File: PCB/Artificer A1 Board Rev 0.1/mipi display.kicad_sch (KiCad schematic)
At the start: 0 parts

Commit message: added a few accessories
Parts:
- added FPC1, FPC2: 0.5K-A-22PB, easyeda:FPC-SMD_22P-P1.00_0.5K-A-22PB, symbol easyeda:0.5K-A-22PB
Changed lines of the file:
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@@
 		(company "Matthew Spotten")
 	)
+	(symbol
+		(lib_id "easyeda:0.5K-A-22PB")
+		(at 158.75 151.13 0)
+		(unit 1)
+		(exclude_from_sim no)
+		(in_bom yes)
+		(on_board yes)
+		(dnp no)
+		(fields_autoplaced yes)
+		(property "Reference" "FPC2"
+			(at 162.56 147.3199 0)
+			(effects
+				(font
+					(size 1.27 1.27)
+				)
+				(justify left)
+			)
+		)
+		(property "Value" "0.5K-A-22PB"
+			(at 162.56 149.8599 0)
+			(effects
+				(font
+					(size 1.27 1.27)
+				)
+				(justify left)
+			)
+		)
+		(property "Footprint" "easyeda:FPC-SMD_22P-P1.00_0.5K-A-22PB"
+			(at 158.75 190.5 0)
+			(effects
+				(font
+					(size 1.27 1.27)
+				)
+				(hide yes)
+			)
+		)
+		(property "Datasheet" ""
+			(at 158.75 151.13 0)
+			(effects
+				(font
+					(size 1.27 1.27)
+				)
+				(hide yes)
+			)
+		)
+		(property "Description" ""
+			(at 158.75 151.13 0)
+			(effects
+				(font
+					(size 1.27 1.27)
+				)
+				(hide yes)
+			)
+		)
+		(property "LCSC Part" "C2914146"
+			(at 158.75 193.04 0)
+			(effects
+				(font
+					(size 1.27 1.27)
+				)
+				(hide yes)
+			)
+		)
+		(pin "14"
+		)
+		(pin "17"
+		)
+		(pin "19"
+		)
+		(pin "3"
+		)
+		(pin "5"
+		)
+		(pin "10"
+		)
+		(pin "1"
+		)
+		(pin "16"
+		)
+		(pin "8"
+		)
+		(pin "6"
+		)
+		(pin "9"
+		)
+		(pin "22"
+		)
+		(pin "12"
+		)
+		(pin "2"
+		)
+		(pin "4"
+		)
+		(pin "7"
+		)
+		(pin "13"
+		)
+		(pin "11"
+		)
+		(pin "15"
+		)
+		(pin "18"
+		)
+		(pin "20"
+		)
+		(pin "21"
+		)
+		(pin "24"
+		)
+		(pin "23"
+		)
+		(instances
+			(project ""
+				(path "/7c37bdb5-94b0-4567-b5ec-a879db855389/f6f33ebb-5c0b-4a90-8c47-ad37181a309f"
+					(reference "FPC2")
+					(unit 1)
+				)
+			)
+		)
+	)
+	(symbol
+		(lib_id "easyeda:0.5K-A-22PB")
+		(at 232.41 60.96 0)
+		(unit 1)
+		(exclude_from_sim no)
+		(in_bom yes)
+		(on_board yes)
+		(dnp no)
+		(fields_autoplaced yes)
+		(property "Reference" "FPC1"
+			(at 236.22 57.1499 0)
+			(effects
+				(font
+					(size 1.27 1.27)
+				)
+				(justify left)
+			)
+		)
+		(property "Value" "0.5K-A-22PB"
+			(at 236.22 59.6899 0)
+			(effects
+				(font
+					(size 1.27 1.27)
+				)
+				(justify left)
+			)
+		)
+		(property "Footprint" "easyeda:FPC-SMD_22P-P1.00_0.5K-A-22PB"
+			(at 232.41 100.33 0)
+			(effects
+				(font
+					(size 1.27 1.27)
+				)
+				(hide yes)
+			)
+		)
+		(property "Datasheet" ""
+			(at 232.41 60.96 0)
+			(effects
+				(font
+					(size 1.27 1.27)
+				)
+				(hide yes)
+			)
+		)
+		(property "Description" ""
+			(at 232.41 60.96 0)
+			(effects
+				(font
+					(size 1.27 1.27)
+				)
+				(hide yes)
+			)
+		)
+		(property "LCSC Part" "C2914146"
+			(at 232.41 102.87 0)
+			(effects
+				(font
+					(size 1.27 1.27)
+				)
+				(hide yes)
+			)
+		)
+		(pin "2"
+		)
+		(pin "6"
+		)
+		(pin "1"
+		)
+		(pin "5"
+		)
+		(pin "12"
+		)
+		(pin "8"
+		)
+		(pin "4"
+		)
+		(pin "3"
+		)
+		(pin "7"
+		)
+		(pin "9"
+		)
+		(pin "10"
+		)
+		(pin "11"
+		)
+		(pin "22"
+		)
+		(pin "24"
+		)
+		(pin "19"
+		)
+		(pin "14"
+		)
+		(pin "15"
+		)
+		(pin "16"
+		)
+		(pin "23"
+		)
+		(pin "17"
+		)
+		(pin "18"
+		)
+		(pin "21"
+		)
+		(pin "20"
+		)
+		(pin "13"
+		)
+		(instances
+			(project ""
+				(path "/7c37bdb5-94b0-4567-b5ec-a879db855389/f6f33ebb-5c0b-4a90-8c47-ad37181a309f"
+					(reference "FPC1")
+					(unit 1)
+				)
+			)
+		)
+	)
 )

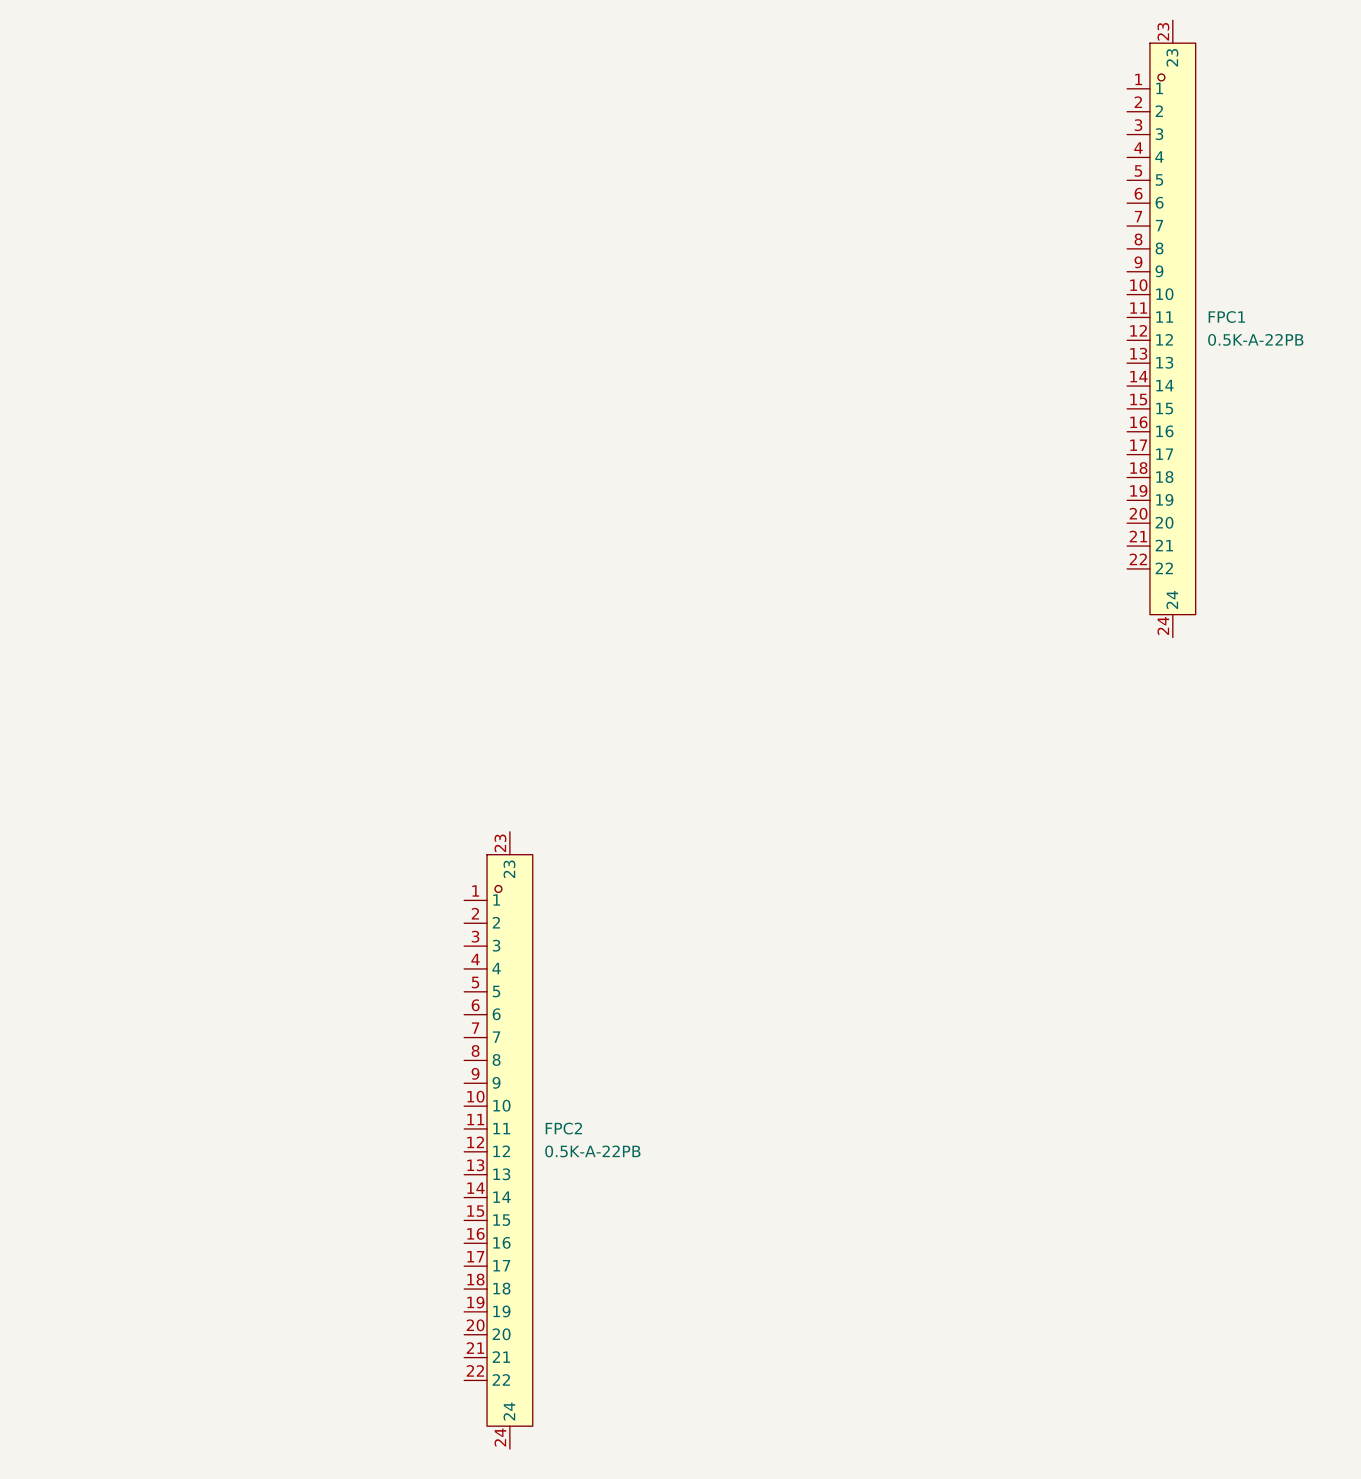
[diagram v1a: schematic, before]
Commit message: added HDMI, DP, DSI, etc
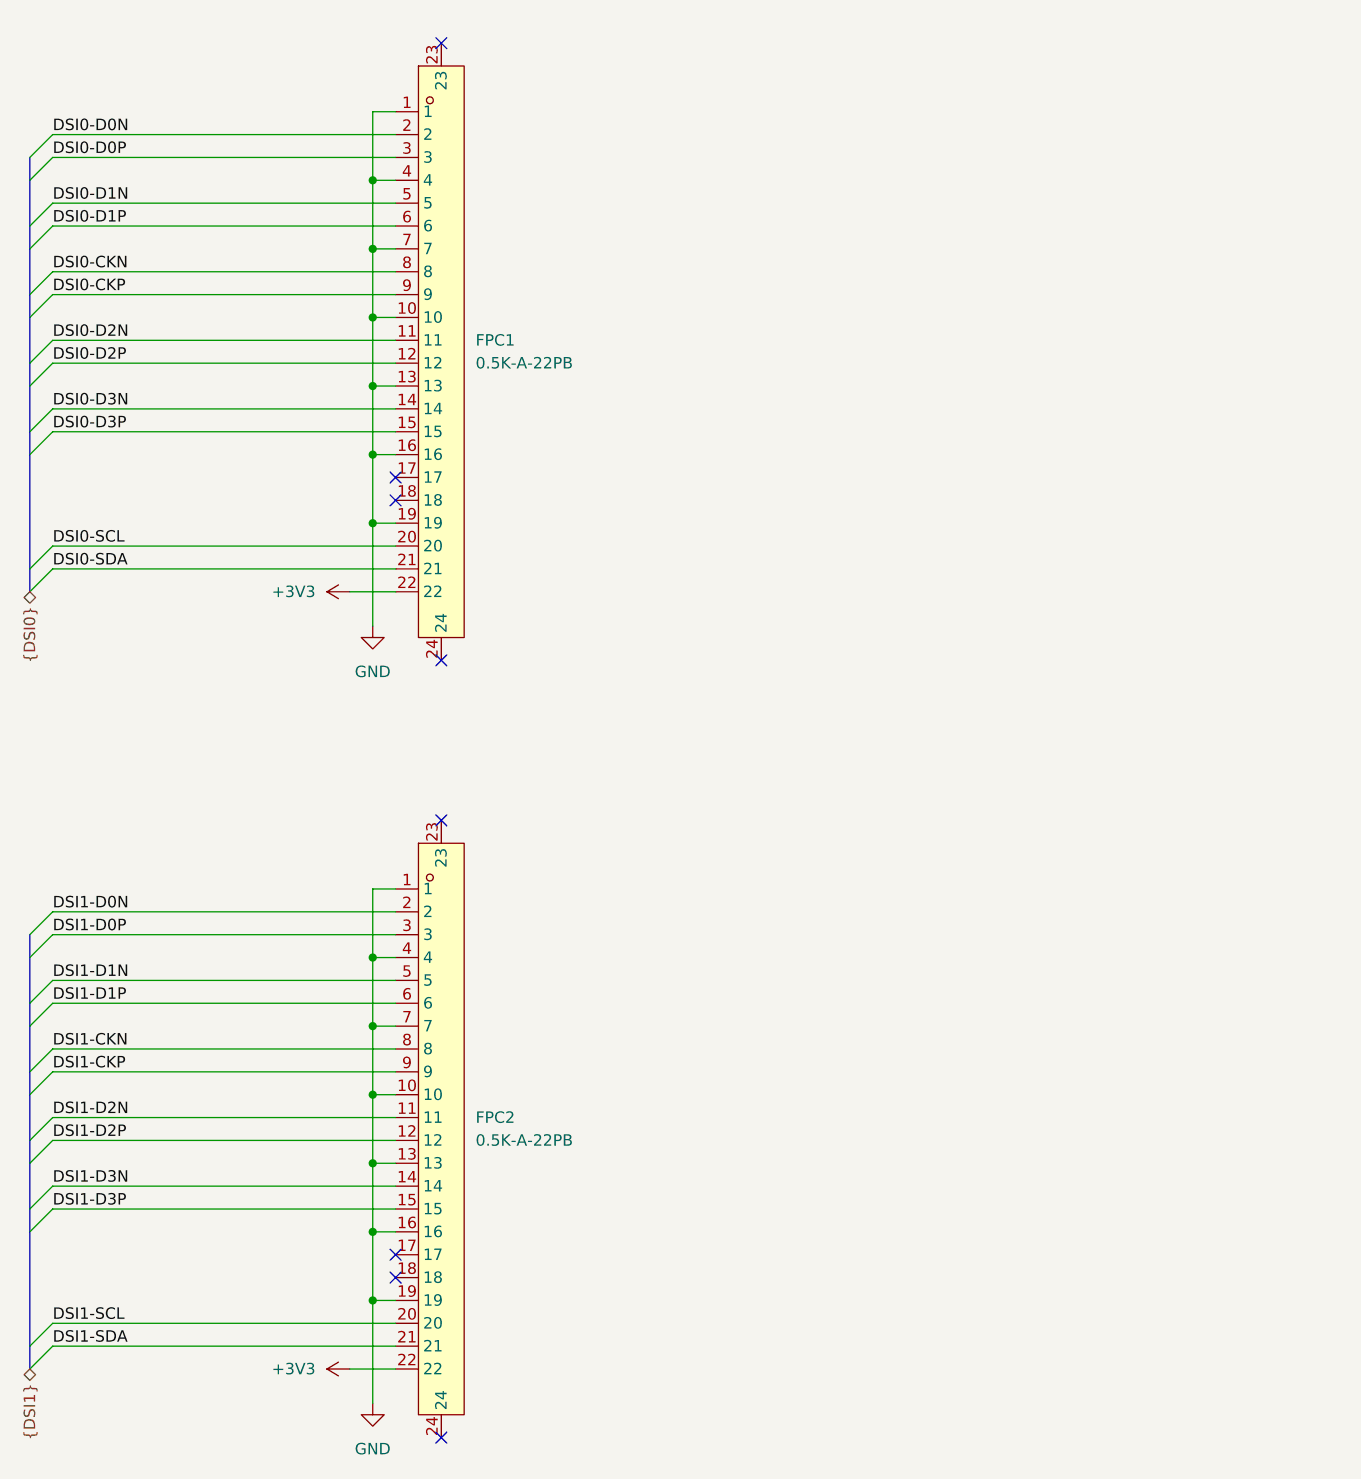
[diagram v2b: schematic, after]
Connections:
- net GND: now reaches FPC2.1
- net GND: now also FPC1.1, FPC1.10, FPC1.13, FPC1.16, FPC1.19, FPC1.4, FPC1.7, FPC2.10, FPC2.13, FPC2.16, FPC2.19, FPC2.4, FPC2.7
- net DSI1-D2N: now reaches FPC2.11
- net DSI1-D2P: now reaches FPC2.12
- net DSI1-D3N: now reaches FPC2.14
- net DSI1-D3P: now reaches FPC2.15
- net DSI1-D0N: now reaches FPC2.2
- net DSI1-SCL: now reaches FPC2.20
- net DSI1-SDA: now reaches FPC2.21
- net +3V3: now reaches FPC2.22
- net +3V3: now also FPC1.22
- net DSI1-D0P: now reaches FPC2.3
- net DSI1-D1N: now reaches FPC2.5
- net DSI1-D1P: now reaches FPC2.6
- net DSI1-CKN: now reaches FPC2.8
- net DSI1-CKP: now reaches FPC2.9
- net DSI0-D2N: now reaches FPC1.11
- net DSI0-D2P: now reaches FPC1.12
- net DSI0-D3N: now reaches FPC1.14
- net DSI0-D3P: now reaches FPC1.15
- net DSI0-D0N: now reaches FPC1.2
- net DSI0-SCL: now reaches FPC1.20
- net DSI0-SDA: now reaches FPC1.21
- net DSI0-D0P: now reaches FPC1.3
- net DSI0-D1N: now reaches FPC1.5
- net DSI0-D1P: now reaches FPC1.6
- net DSI0-CKN: now reaches FPC1.8
- net DSI0-CKP: now reaches FPC1.9
- no-connect marks 0 -> 8
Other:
- moved on the sheet: FPC1, FPC2
